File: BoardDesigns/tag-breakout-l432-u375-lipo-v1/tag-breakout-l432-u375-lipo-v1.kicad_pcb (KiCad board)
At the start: 2 copper layers, 53.3 x 73.7 mm, 44 parts, among them J1 Conn_01x04_Female, J102 Conn_02x05_Odd_Even, J104 USB_B_Mini, J2 Conn_01x02_Male, J3 Conn_01x17, J4 Conn_01x17, J5 Conn_01x02_Male, Q1 Q_NPN_BEC, U1 XC6206, U10 AP2112K-1.8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

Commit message: update design
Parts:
- added C102: 0.1uF, Capacitor_SMD:C_0402_1005Metric, F.Cu at (124.3, 63.8)
- added C103: 0.1uF, Capacitor_SMD:C_0402_1005Metric, F.Cu at (128.9, 79.7)
- added C109: 0.1uF, Capacitor_SMD:C_0402_1005Metric, F.Cu at (133.1, 79.7)
- added C110: 0.1uF, Capacitor_SMD:C_0402_1005Metric, F.Cu at (129.4, 75.1)
- added C111: 0.1uF, Capacitor_SMD:C_0402_1005Metric, F.Cu at (133.4, 75.2)
- added FID1: Fiducial, Fiducial:Fiducial_0.5mm_Mask1mm, F.Cu at (104.1, 53.3)
- added FID2: Fiducial, Fiducial:Fiducial_0.5mm_Mask1mm, F.Cu at (152.4, 53.3)
- added FID3: Fiducial, Fiducial:Fiducial_0.5mm_Mask1mm, F.Cu at (152.4, 121.9)
- added U4: USBLC6-2P6, Package_TO_SOT_SMD:SOT-666, F.Cu at (126.1, 63.8)
- D1: footprint LED_SMD:LED_0603_1608Metric -> LED_SMD:LED_0805_2012Metric
- R1: value 510 -> 100
- R107: value 510 -> 200
- moved U7 1.41 mm to (128.2, 77.2)
- moved U8 0.66 mm to (132.4, 77.2)
- moved R106 0.46 mm to (131.8, 79.8)
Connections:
- J1 pad 3: EXT_PWR -> unconnected-(J1-Pin_3-Pad3)
- J104 pad 2: /USB_DM -> /DM
- J104 pad 3: /USB_DP -> /DP
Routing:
- net VUSB: track 26.3 -> 33.7 mm
- net /USB_DM: track 11.8 -> 4.86 mm
- net /USB_DP: track 12.2 -> 5.60 mm
- net GND: track 57.0 -> 63.4 mm, vias 29 -> 68
- net /DP: track 0.00 -> 6.00 mm
- net /DM: track 0.00 -> 5.42 mm
- net +1V8: track 22.0 -> 25.7 mm
- net +3V3: track 83.4 -> 85.9 mm, vias 5 -> 6
- net Net-(J5-Pin_2): track 7.49 -> 8.64 mm
- net /UART_TX: track 20.8 -> 21.5 mm
- net TAG_1V8: track 83.6 -> 83.0 mm
- net Net-(U5-PA15): track 9.65 -> 10.3 mm
- net Net-(J5-Pin_1): track 7.77 -> 8.43 mm
- net (no net): vias 0 -> 1

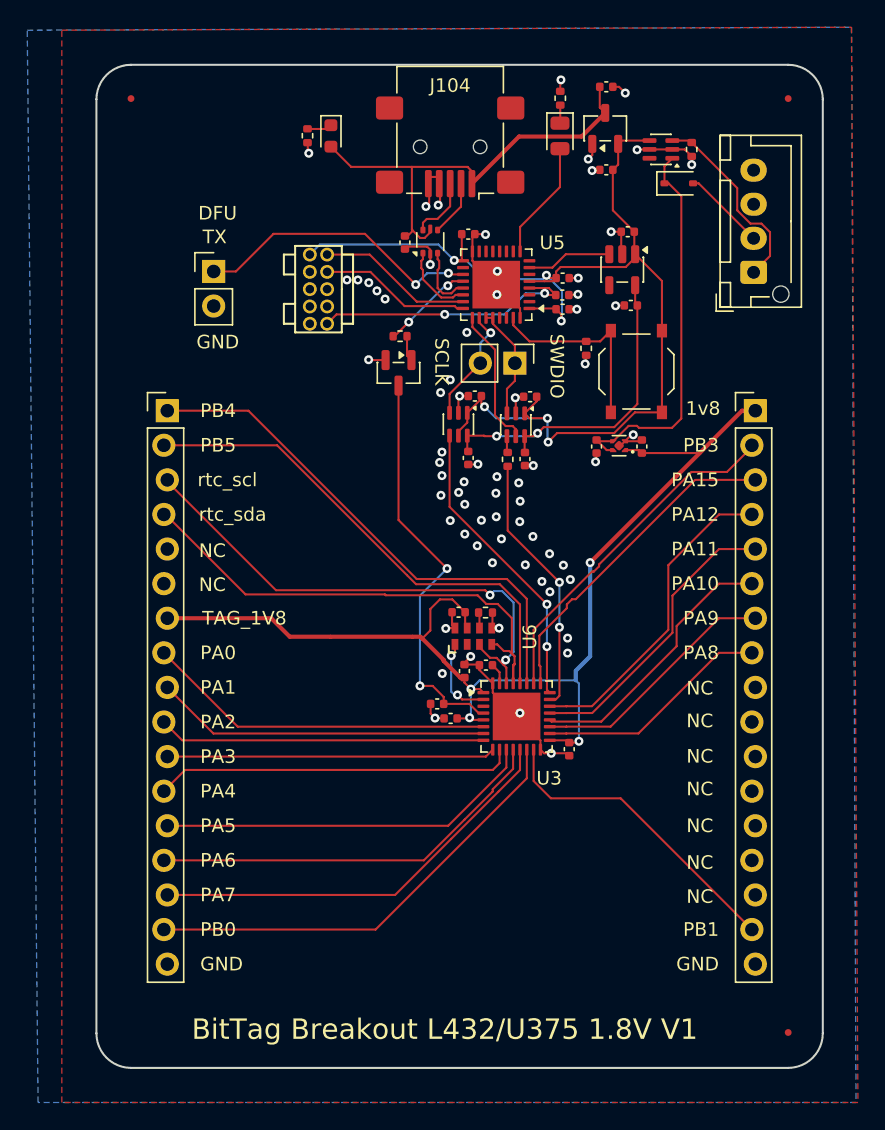
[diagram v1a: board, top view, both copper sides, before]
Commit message: check in 2 layer board
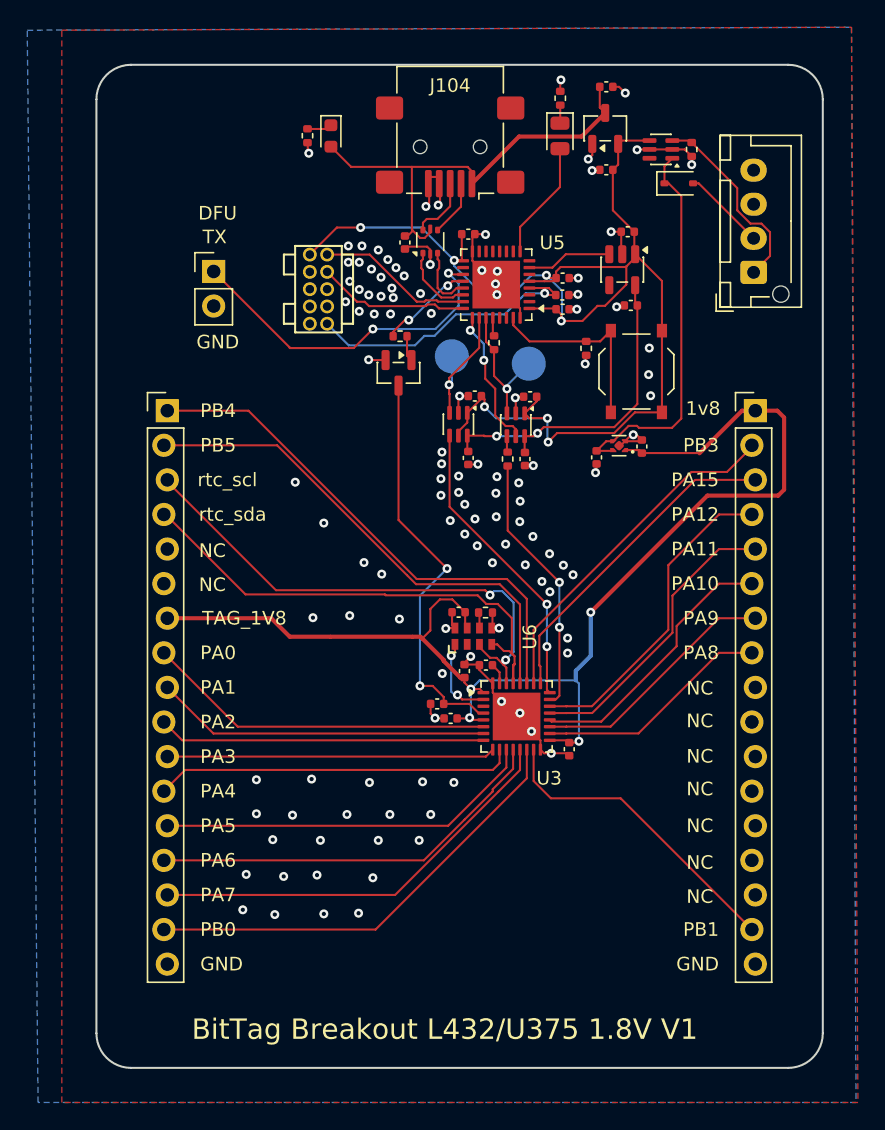
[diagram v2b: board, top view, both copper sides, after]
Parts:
- removed FID1, FID2, FID3: Fiducial, Fiducial:Fiducial_0.5mm_Mask1mm
- removed J5: Conn_01x02_Male, Connector_PinHeader_2.54mm:PinHeader_1x02_P2.54mm_Vertical
- added R2: 100, Resistor_SMD:R_0402_1005Metric, F.Cu at (130.8, 71.2)
- added TP1: TestPoint, TestPoint:TestPoint_Pad_D2.5mm, B.Cu at (133.3, 72.8)
- added TP2: TestPoint, TestPoint:TestPoint_Pad_D2.5mm, B.Cu at (127.7, 72.2)
- R106: value 200 -> 100
- moved C108 0.80 mm to (138.3, 79.6)
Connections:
- U5 pad 27: Net-(J5-Pin_1) -> Net-(U5-PB4)
- U5 pad 28: Net-(J5-Pin_1) -> Net-(U5-PB5)
- U8 pad 3: Net-(J5-Pin_1) -> Net-(U5-PB4)
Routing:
- net TAG_1V8: track 83.0 -> 93.9 mm
- net Net-(U5-PB4): track 0.00 -> 10.2 mm, vias 0 -> 1
- net +3V3: track 85.9 -> 95.9 mm, vias 6 -> 7
- net Net-(J5-Pin_1): track 8.43 -> 0.00 mm
- net /UART_TX: track 21.5 -> 25.5 mm
- net Net-(U5-PB3): track 8.64 -> 10.1 mm
- net Net-(U5-PB5): track 0.00 -> 1.36 mm
- net /NRST: track 19.9 -> 21.2 mm, vias 2 -> 1
- net GND: track 63.4 -> 64.1 mm, vias 68 -> 119
- net Net-(U5-PA15): track 10.3 -> 10.4 mm, vias 0 -> 2
- net (no net): vias 1 -> 0

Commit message: final layout tweaking of tag-breakout-l432-u375-lipo-v1
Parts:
- moved R3 7.48 mm to (123.4, 94.2), turned to -90 degrees
- moved C7 7.08 mm to (123.4, 96.2), turned to -90 degrees
- moved U6 4.76 mm to (125.1, 95.1), turned to 180 degrees
- moved C110 2.18 mm to (130.0, 77.2), turned to -90 degrees
- moved C111 1.77 mm to (134.2, 76.8), turned to -90 degrees
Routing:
- net TAG_1V8: track 93.9 -> 14.4 mm, vias 4 -> 5
- net +3V3: track 95.9 -> 28.6 mm, vias 7 -> 9
- net /stm32/rtc_sda: track 37.0 -> 32.4 mm
- net /UART_TX: track 25.5 -> 21.2 mm
- net /stm32/rtc_scl: track 38.3 -> 34.3 mm
- net /stm32/NRST: track 30.1 -> 28.4 mm
- net /stm32/clkout: track 6.20 -> 5.01 mm, vias 2 -> 0
- net /NRST: track 21.2 -> 20.3 mm
- net /USB_DM: track 4.86 -> 4.26 mm
- net /stm32/PB3: track 25.7 -> 26.0 mm, vias 0 -> 2
- net TAG_SCK: vias 2 -> 0
- net /stm32/PA15: vias 0 -> 2
- net GND: vias 119 -> 53
- net TAG_SWDIO: vias 2 -> 0
- added copper zone on In2.Cu, net +3V3
- added copper zone on In1.Cu, net GND
- added copper zone on In2.Cu, net TAG_1V8
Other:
- copper layers 2 -> 4

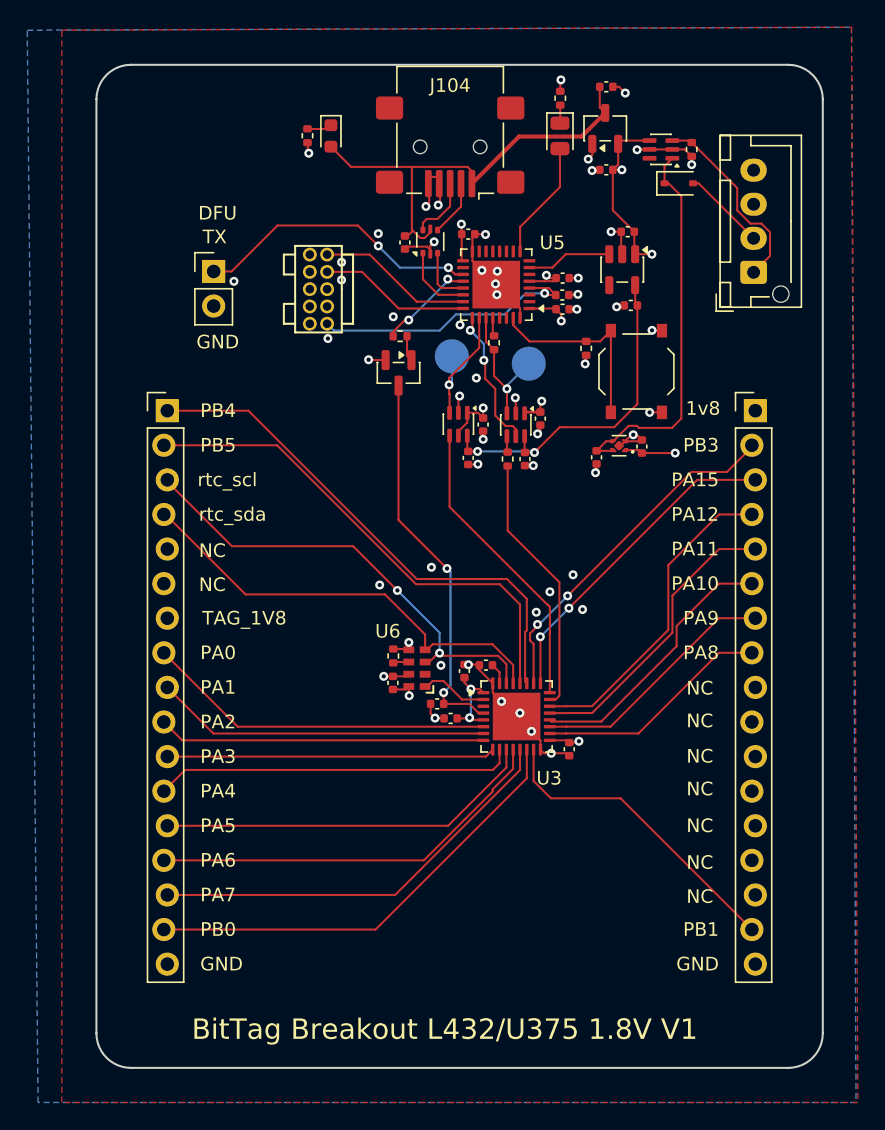
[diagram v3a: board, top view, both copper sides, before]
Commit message: Update IMU breakout and bittag base designs
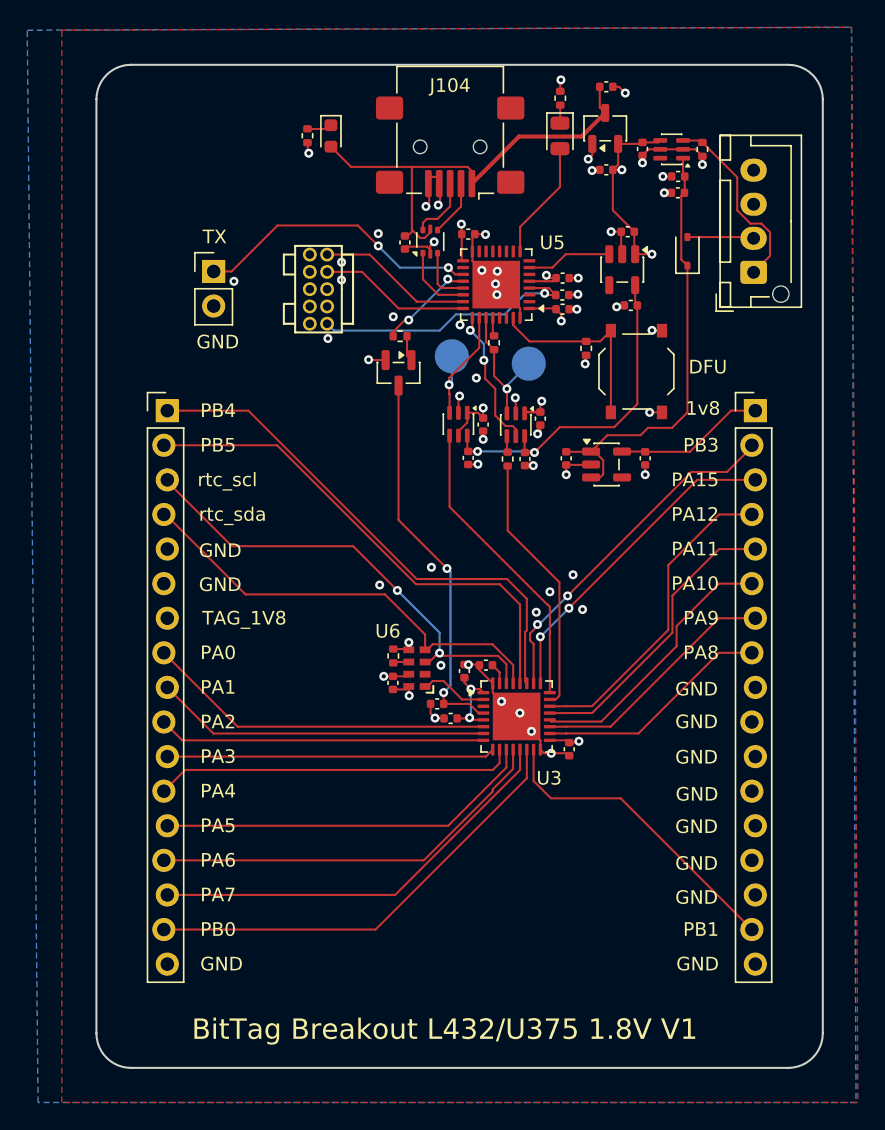
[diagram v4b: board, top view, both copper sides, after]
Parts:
- added C112: 1uF, Capacitor_SMD:C_0402_1005Metric, F.Cu at (141.7, 57.0)
- added C113: 0.1uF, Capacitor_SMD:C_0402_1005Metric, F.Cu at (144.3, 59.0)
- added C114: 1uF, Capacitor_SMD:C_0402_1005Metric, F.Cu at (144.3, 60.2)
- U11: value TPS7A0218PDQNR -> TPS7A0218PDBVR; footprint Package_SON:Texas_X2SON-4_1x1mm_P0.65mm -> Package_TO_SOT_SMD:SOT-23-5
- moved D4 5.04 mm to (145.0, 64.5), turned to 90 degrees
- moved C108 2.23 mm to (136.1, 79.7)
- moved U11 1.66 mm to (139.1, 80.2), turned to 0 degrees
- moved C106 0.90 mm to (141.9, 79.7), turned to -90 degrees
- moved R7 0.79 mm to (146.1, 57.0)
- moved U2 0.79 mm to (143.8, 57.0)
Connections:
- J3 pad 5: /stm32/PB8 -> GND
- J3 pad 6: /stm32/PB9 -> GND
- J4 pad 10: /stm32/PB14 -> GND
- J4 pad 11: /stm32/PB13 -> GND
- J4 pad 12: /stm32/PB12 -> GND
- J4 pad 13: /stm32/PB11 -> GND
- J4 pad 14: /stm32/PB10 -> GND
- J4 pad 15: /stm32/PB2 -> GND
- J4 pad 9: /stm32/PB15 -> GND
- U11 pad 1: TAG_1V8 -> TAG_3V3
- U11 pad 4: TAG_3V3 -> unconnected-(U11-NC-Pad4)
- U11 pad 5: GND -> TAG_1V8
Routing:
- net TAG_1V8: track 14.4 -> 21.7 mm, vias 5 -> 4
- net TAG_3V3: track 28.6 -> 32.3 mm
- net GND: track 64.1 -> 65.7 mm, vias 53 -> 55
- net PWR_IN: track 6.12 -> 4.90 mm
- net +3V3: track 28.6 -> 29.8 mm
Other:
- board text removed: "NC"
